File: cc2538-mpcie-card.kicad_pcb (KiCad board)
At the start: 2 copper layers, 30.1 x 50.8 mm, 27 parts, among them J1 Bus_PCI_Express_Mini, J2 Conn_ARM_JTAG_SWD_10, Q1 MUN5214DW1, Q2 MUN5214DW1, U1 CC2538_SZ12, U2 CP2102N-A01-GQFN24

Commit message: Fix up component values
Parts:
- C8: value 1uF -> 10uF
- R3: value 1K -> 200R
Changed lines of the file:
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@@
       (effects (font (size 0.8 0.8) (thickness 0.1)))
     )
-    (fp_text value 1K (at 0 1.43 90) (layer F.Fab)
+    (fp_text value 200R (at 0 1.43 90) (layer F.Fab)
       (effects (font (size 1 1) (thickness 0.15)))
     )
@@
       (effects (font (size 0.8 0.8) (thickness 0.1)))
     )
-    (fp_text value 1uF (at 0 1.43 90) (layer F.Fab)
+    (fp_text value 10uF (at 0 1.43 90) (layer F.Fab)
       (effects (font (size 1 1) (thickness 0.15)))
     )

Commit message: Added document title & rev, and more GND vias
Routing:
- net GND: vias 42 -> 50
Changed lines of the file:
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@@
     (thickness 1.6)
     (drawings 40)
-    (tracks 278)
+    (tracks 286)
     (zones 0)
     (modules 27)
@@
   )
   (page A4)
+  (title_block
+    (title "CC2538 Zigbee mPCIe")
+    (rev 2021.04)
+  )
   (layers
     (0 F.Cu signal)
@@
   (via (at 132.55 138.95) (size 0.6) (drill 0.3) (layers F.Cu B.Cu) (net 1))
   (via (at 132.4 144.05) (size 0.6) (drill 0.3) (layers F.Cu B.Cu) (net 1))
+  (via (at 132.7 113.3) (size 0.6) (drill 0.3) (layers F.Cu B.Cu) (net 1))
+  (via (at 138.08 113.3) (size 0.6) (drill 0.3) (layers F.Cu B.Cu) (net 1))
+  (via (at 143.46 113.3) (size 0.6) (drill 0.3) (layers F.Cu B.Cu) (net 1))
+  (via (at 148.84 113.3) (size 0.6) (drill 0.3) (layers F.Cu B.Cu) (net 1))
+  (via (at 154.22 113.3) (size 0.6) (drill 0.3) (layers F.Cu B.Cu) (net 1))
+  (via (at 159.6 113.3) (size 0.6) (drill 0.3) (layers F.Cu B.Cu) (net 1))
+  (via (at 132.7 118.2) (size 0.6) (drill 0.3) (layers F.Cu B.Cu) (net 1))
+  (via (at 132.4 123.2) (size 0.6) (drill 0.3) (layers F.Cu B.Cu) (net 1))
   (segment (start 149.3 150.4) (end 149.3 148.35) (width 0.2) (layer B.Cu) (net 2) (status 10))
   (segment (start 149.3 148.35) (end 148.8 147.85) (width 0.2) (layer B.Cu) (net 2))

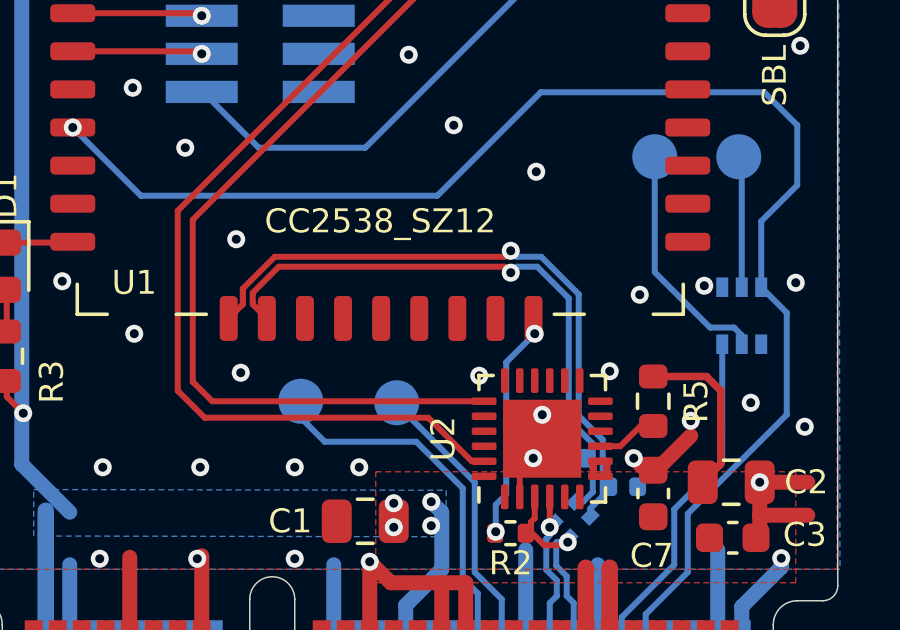
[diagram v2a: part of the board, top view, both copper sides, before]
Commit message: Totally forgot to connect RXD/TXD serial lines
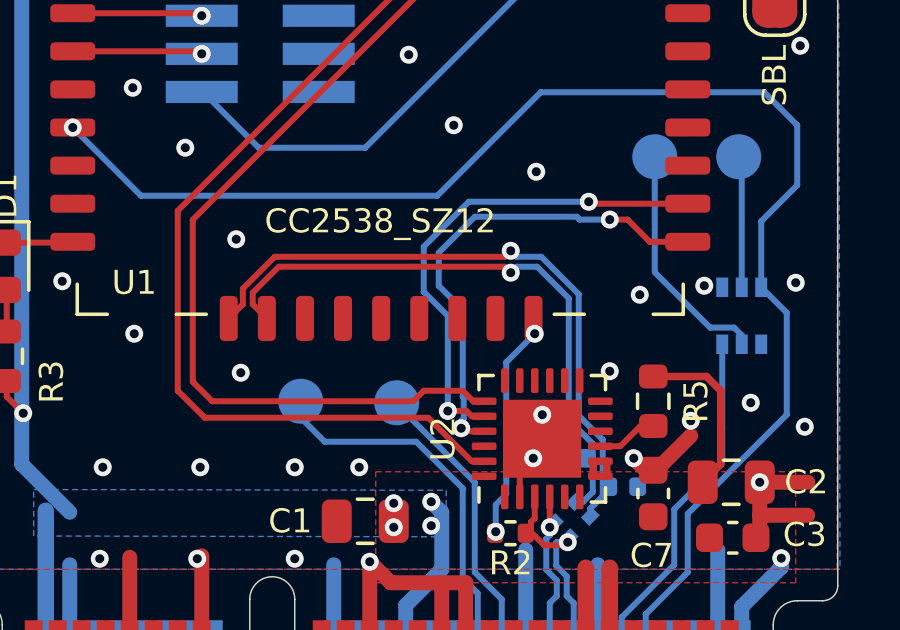
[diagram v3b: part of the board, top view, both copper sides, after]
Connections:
- U1 pad 22: (no net) -> /CC_RX
- U1 pad 23: (no net) -> /CC_TX
- U2 pad 20: (no net) -> /CC_TX
- U2 pad 21: (no net) -> /CC_RX
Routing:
- net /CC_TX: track 0.00 -> 16.5 mm, vias 0 -> 2
- net /CC_RX: track 0.00 -> 16.2 mm, vias 0 -> 2
- net GND: vias 50 -> 49
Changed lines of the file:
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@@
     (thickness 1.6)
     (drawings 40)
-    (tracks 286)
+    (tracks 319)
     (zones 0)
     (modules 27)
-    (nets 25)
+    (nets 27)
   )
   (page A4)
@@
   (net 23 "Net-(D1-Pad2)")
   (net 24 /~LED_PWR)
+  (net 25 /CC_RX)
+  (net 26 /CC_TX)
   (net_class Default "This is the default net class."
     (clearance 0.13)
@@
     (add_net +3V3)
     (add_net /CC_RST)
+    (add_net /CC_RX)
     (add_net /CC_SBL)
+    (add_net /CC_TX)
     (add_net /CC_USB+)
     (add_net /CC_USB-)
@@
     (pad 19 smd roundrect (at 1.25 -1.9375 90) (size 0.25 0.825) (layers F.Cu F.Paste F.Mask) (roundrect_rratio 0.25)
       (net 17 "Net-(Q2-Pad1)"))
-    (pad 20 smd roundrect (at 0.75 -1.9375 90) (size 0.25 0.825) (layers F.Cu F.Paste F.Mask) (roundrect_rratio 0.25))
-    (pad 21 smd roundrect (at 0.25 -1.9375 90) (size 0.25 0.825) (layers F.Cu F.Paste F.Mask) (roundrect_rratio 0.25))
+    (pad 20 smd roundrect (at 0.75 -1.9375 90) (size 0.25 0.825) (layers F.Cu F.Paste F.Mask) (roundrect_rratio 0.25)
+      (net 26 /CC_TX))
+    (pad 21 smd roundrect (at 0.25 -1.9375 90) (size 0.25 0.825) (layers F.Cu F.Paste F.Mask) (roundrect_rratio 0.25)
+      (net 25 /CC_RX))
     (pad 22 smd roundrect (at -0.25 -1.9375 90) (size 0.25 0.825) (layers F.Cu F.Paste F.Mask) (roundrect_rratio 0.25))
     (pad 23 smd roundrect (at -0.75 -1.9375 90) (size 0.25 0.825) (layers F.Cu F.Paste F.Mask) (roundrect_rratio 0.25)
@@
     (pad 12 smd roundrect (at -10.25 6.985 270) (size 0.6 1.5) (layers F.Cu F.Paste F.Mask) (roundrect_rratio 0.25)
       (net 24 /~LED_PWR))
-    (pad 22 smd roundrect (at 10.25 6.985 270) (size 0.6 1.5) (layers F.Cu F.Paste F.Mask) (roundrect_rratio 0.25))
-    (pad 23 smd roundrect (at 10.25 5.715 270) (size 0.6 1.5) (layers F.Cu F.Paste F.Mask) (roundrect_rratio 0.25))
+    (pad 22 smd roundrect (at 10.25 6.985 270) (size 0.6 1.5) (layers F.Cu F.Paste F.Mask) (roundrect_rratio 0.25)
+      (net 25 /CC_RX))
+    (pad 23 smd roundrect (at 10.25 5.715 270) (size 0.6 1.5) (layers F.Cu F.Paste F.Mask) (roundrect_rratio 0.25)
+      (net 26 /CC_TX))
     (pad 24 smd roundrect (at 10.25 4.445 270) (size 0.6 1.5) (layers F.Cu F.Paste F.Mask) (roundrect_rratio 0.25))
     (pad 25 smd roundrect (at 10.25 3.175 270) (size 0.6 1.5) (layers F.Cu F.Paste F.Mask) (roundrect_rratio 0.25))
@@
   (via (at 140.05 144.15) (size 0.6) (drill 0.3) (layers F.Cu B.Cu) (net 1))
   (via (at 136.8 144.15) (size 0.6) (drill 0.3) (layers F.Cu B.Cu) (net 1))
-  (via (at 149.35 141.1) (size 0.6) (drill 0.3) (layers F.Cu B.Cu) (net 1))
   (via (at 151.45 142.4) (size 0.6) (drill 0.3) (layers F.Cu B.Cu) (net 1) (status 30))
   (via (at 151.15 143.85) (size 0.6) (drill 0.3) (layers F.Cu B.Cu) (net 1) (status 30))
@@
   (segment (start 159.4 121) (end 160.15 121) (width 0.2) (layer F.Cu) (net 16) (status 20))
   (segment (start 158.75 120.35) (end 159.4 121) (width 0.2) (layer F.Cu) (net 16))
-  (segment (start 149.5125 141.95) (end 140.45 141.95) (width 0.2) (layer F.Cu) (net 17) (status 10))
   (segment (start 140.45 141.95) (end 139.8 141.3) (width 0.2) (layer F.Cu) (net 17))
   (segment (start 139.8 141.3) (end 139.8 135.9) (width 0.2) (layer F.Cu) (net 17))
@@
   (segment (start 160.1 121.6) (end 160.15 121.65) (width 0.2) (layer F.Cu) (net 17) (status 30))
   (segment (start 159.375 121.6) (end 160.1 121.6) (width 0.2) (layer F.Cu) (net 17) (status 20))
+  (segment (start 140.45 141.95) (end 147.15 141.95) (width 0.2) (layer F.Cu) (net 17))
+  (segment (start 147.15 141.95) (end 147.5 141.6) (width 0.2) (layer F.Cu) (net 17))
+  (segment (start 147.5 141.6) (end 148.8 141.6) (width 0.2) (layer F.Cu) (net 17))
+  (segment (start 149.15 141.95) (end 149.5125 141.95) (width 0.2) (layer F.Cu) (net 17))
+  (segment (start 148.8 141.6) (end 149.15 141.95) (width 0.2) (layer F.Cu) (net 17))
   (via (at 149.9 146.3) (size 0.6) (drill 0.3) (layers F.Cu B.Cu) (net 18) (status 30))
   (segment (start 149.88 146.32) (end 149.9 146.3) (width 0.2) (layer F.Cu) (net 18) (status 30))
@@
   (segment (start 135.7725 136.6625) (end 135.8 136.635) (width 0.2) (layer F.Cu) (net 24) (status 30))
   (segment (start 133.6 136.6625) (end 135.7725 136.6625) (width 0.2) (layer F.Cu) (net 24) (status 30))
+  (via (at 148.749767 142.850233) (size 0.6) (drill 0.3) (layers F.Cu B.Cu) (net 25))
+  (segment (start 148.849534 142.95) (end 148.749767 142.850233) (width 0.2) (layer F.Cu) (net 25))
+  (segment (start 149.5125 142.95) (end 148.849534 142.95) (width 0.2) (layer F.Cu) (net 25))
+  (segment (start 148.831921 142.528148) (end 148.831921 141.831921) (width 0.2) (layer B.Cu) (net 25))
+  (segment (start 148.749767 142.610302) (end 148.831921 142.528148) (width 0.2) (layer B.Cu) (net 25))
+  (segment (start 148.749767 142.850233) (end 148.749767 142.610302) (width 0.2) (layer B.Cu) (net 25))
+  (segment (start 148.831921 141.831921) (end 148.8 141.8) (width 0.2) (layer B.Cu) (net 25))
+  (segment (start 148.8 141.8) (end 148.8 138.9) (width 0.2) (layer B.Cu) (net 25))
+  (segment (start 148.8 138.9) (end 148 138.1) (width 0.2) (layer B.Cu) (net 25))
+  (segment (start 148 138.1) (end 148 137) (width 0.2) (layer B.Cu) (net 25))
+  (segment (start 148 137) (end 149.2 135.8) (width 0.2) (layer B.Cu) (net 25))
+  (segment (start 156.3 136.635) (end 155.035 136.635) (width 0.2) (layer F.Cu) (net 25))
+  (via (at 153.7 135.895) (size 0.6) (drill 0.3) (layers F.Cu B.Cu) (net 25))
+  (segment (start 154.295 135.895) (end 153.7 135.895) (width 0.2) (layer F.Cu) (net 25))
+  (segment (start 155.035 136.635) (end 154.295 135.895) (width 0.2) (layer F.Cu) (net 25))
+  (segment (start 149.2 135.8) (end 152.6 135.8) (width 0.2) (layer B.Cu) (net 25))
+  (segment (start 152.695 135.895) (end 153.7 135.895) (width 0.2) (layer B.Cu) (net 25))
+  (segment (start 152.6 135.8) (end 152.695 135.895) (width 0.2) (layer B.Cu) (net 25))
+  (via (at 148.30192 142.273747) (size 0.6) (drill 0.3) (layers F.Cu B.Cu) (net 26))
+  (segment (start 148.923747 142.273747) (end 148.30192 142.273747) (width 0.2) (layer F.Cu) (net 26))
+  (segment (start 149.1 142.45) (end 148.923747 142.273747) (width 0.2) (layer F.Cu) (net 26))
+  (segment (start 149.5125 142.45) (end 149.1 142.45) (width 0.2) (layer F.Cu) (net 26))
+  (segment (start 148.30192 142.273747) (end 148.30192 139.10192) (width 0.2) (layer B.Cu) (net 26))
+  (segment (start 148.30192 139.10192) (end 147.5 138.3) (width 0.2) (layer B.Cu) (net 26))
+  (segment (start 147.5 138.3) (end 147.5 136.8) (width 0.2) (layer B.Cu) (net 26))
+  (segment (start 147.5 136.8) (end 149 135.3) (width 0.2) (layer B.Cu) (net 26))
+  (segment (start 149 135.3) (end 153 135.3) (width 0.2) (layer B.Cu) (net 26))
+  (via (at 153 135.3) (size 0.6) (drill 0.3) (layers F.Cu B.Cu) (net 26))
+  (segment (start 153.065 135.365) (end 153 135.3) (width 0.2) (layer F.Cu) (net 26))
+  (segment (start 156.3 135.365) (end 153.065 135.365) (width 0.2) (layer F.Cu) (net 26))
   (zone (net 8) (net_name +3V3) (layer B.Cu) (hatch edge 0.508)
     (priority 1)

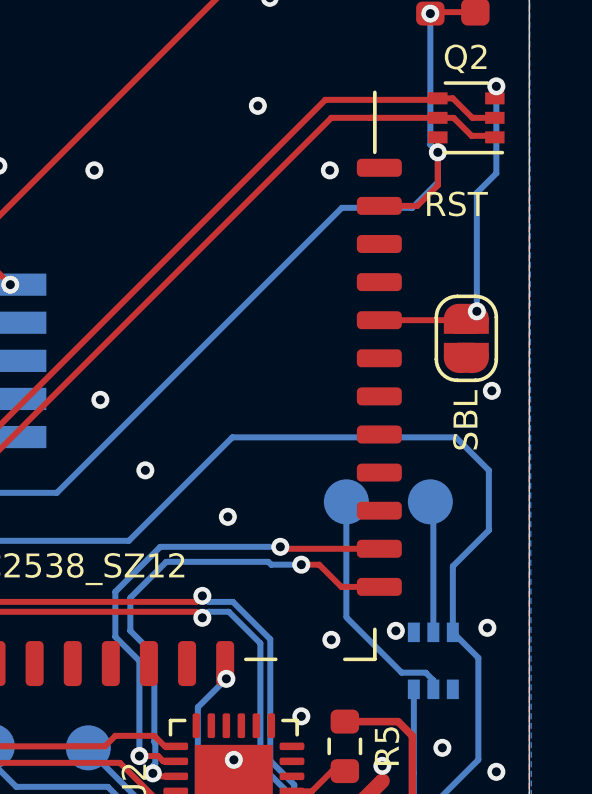
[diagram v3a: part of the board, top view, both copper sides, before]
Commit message: Added RX/TX marking to module
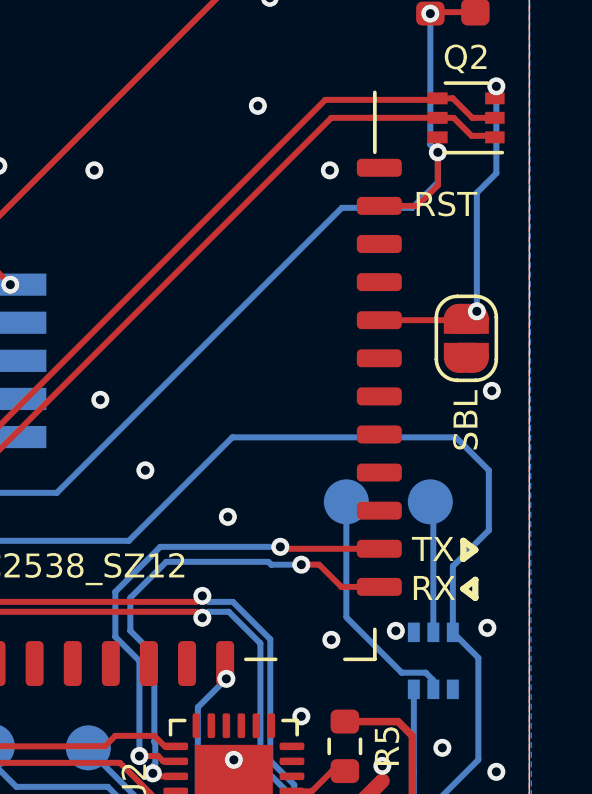
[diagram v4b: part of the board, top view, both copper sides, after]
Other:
- board text added: "RX"
- board text added: "TX"
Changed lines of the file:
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@@
   (general
     (thickness 1.6)
-    (drawings 40)
+    (drawings 48)
     (tracks 319)
     (zones 0)
@@
     )
   )
+  (gr_line (start 159.5 137) (end 159.1 136.7) (layer F.SilkS) (width 0.21))
+  (gr_line (start 159.5 137) (end 159.5 136.4) (layer F.SilkS) (width 0.21))
+  (gr_line (start 159.5 136.4) (end 159.1 136.7) (layer F.SilkS) (width 0.21))
+  (gr_text RX (at 158.1 136.7) (layer F.SilkS)
+    (effects (font (size 0.8 0.8) (thickness 0.1)))
+  )
+  (gr_line (start 159.1 135.1) (end 159.5 135.4) (layer F.SilkS) (width 0.21))
+  (gr_line (start 159.1 135.7) (end 159.5 135.4) (layer F.SilkS) (width 0.21))
+  (gr_line (start 159.1 135.1) (end 159.1 135.7) (layer F.SilkS) (width 0.21))
+  (gr_text TX (at 158.1 135.4) (layer F.SilkS)
+    (effects (font (size 0.8 0.8) (thickness 0.1)))
+  )
   (gr_text "PCB thickness: 1.00mm" (at 146.275 153.24) (layer Dwgs.User)
     (effects (font (size 1 1) (thickness 0.15)))
@@
     (effects (font (size 1 1) (thickness 0.15)))
   )
-  (gr_text RST (at 158.85 123.9) (layer F.SilkS)
+  (gr_text RST (at 158.5 123.9) (layer F.SilkS)
     (effects (font (size 0.8 0.8) (thickness 0.1)))
   )
